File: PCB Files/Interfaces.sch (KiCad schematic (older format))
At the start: 22 parts

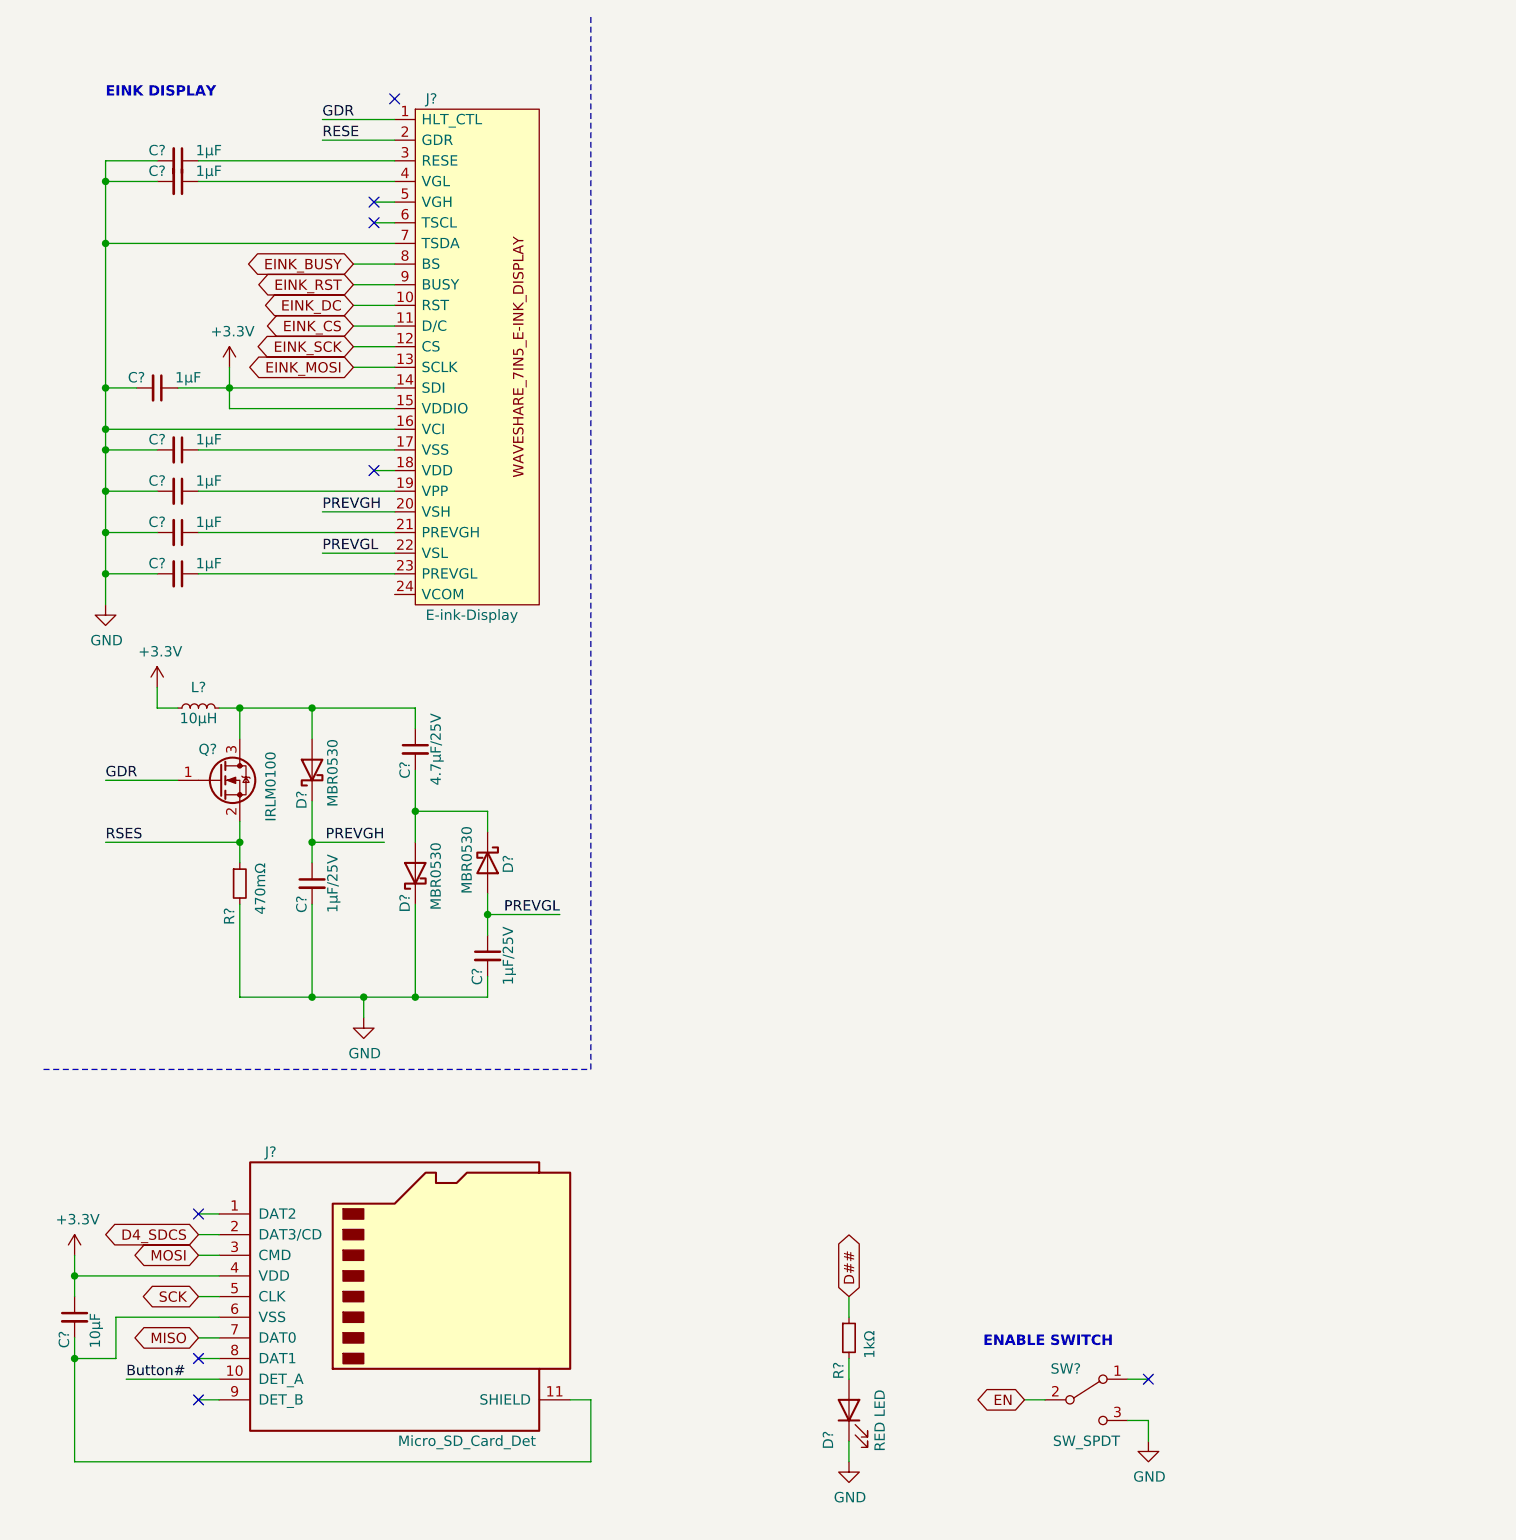
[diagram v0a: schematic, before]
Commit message: Added buttons, aux power distribution and connections to PI Pico
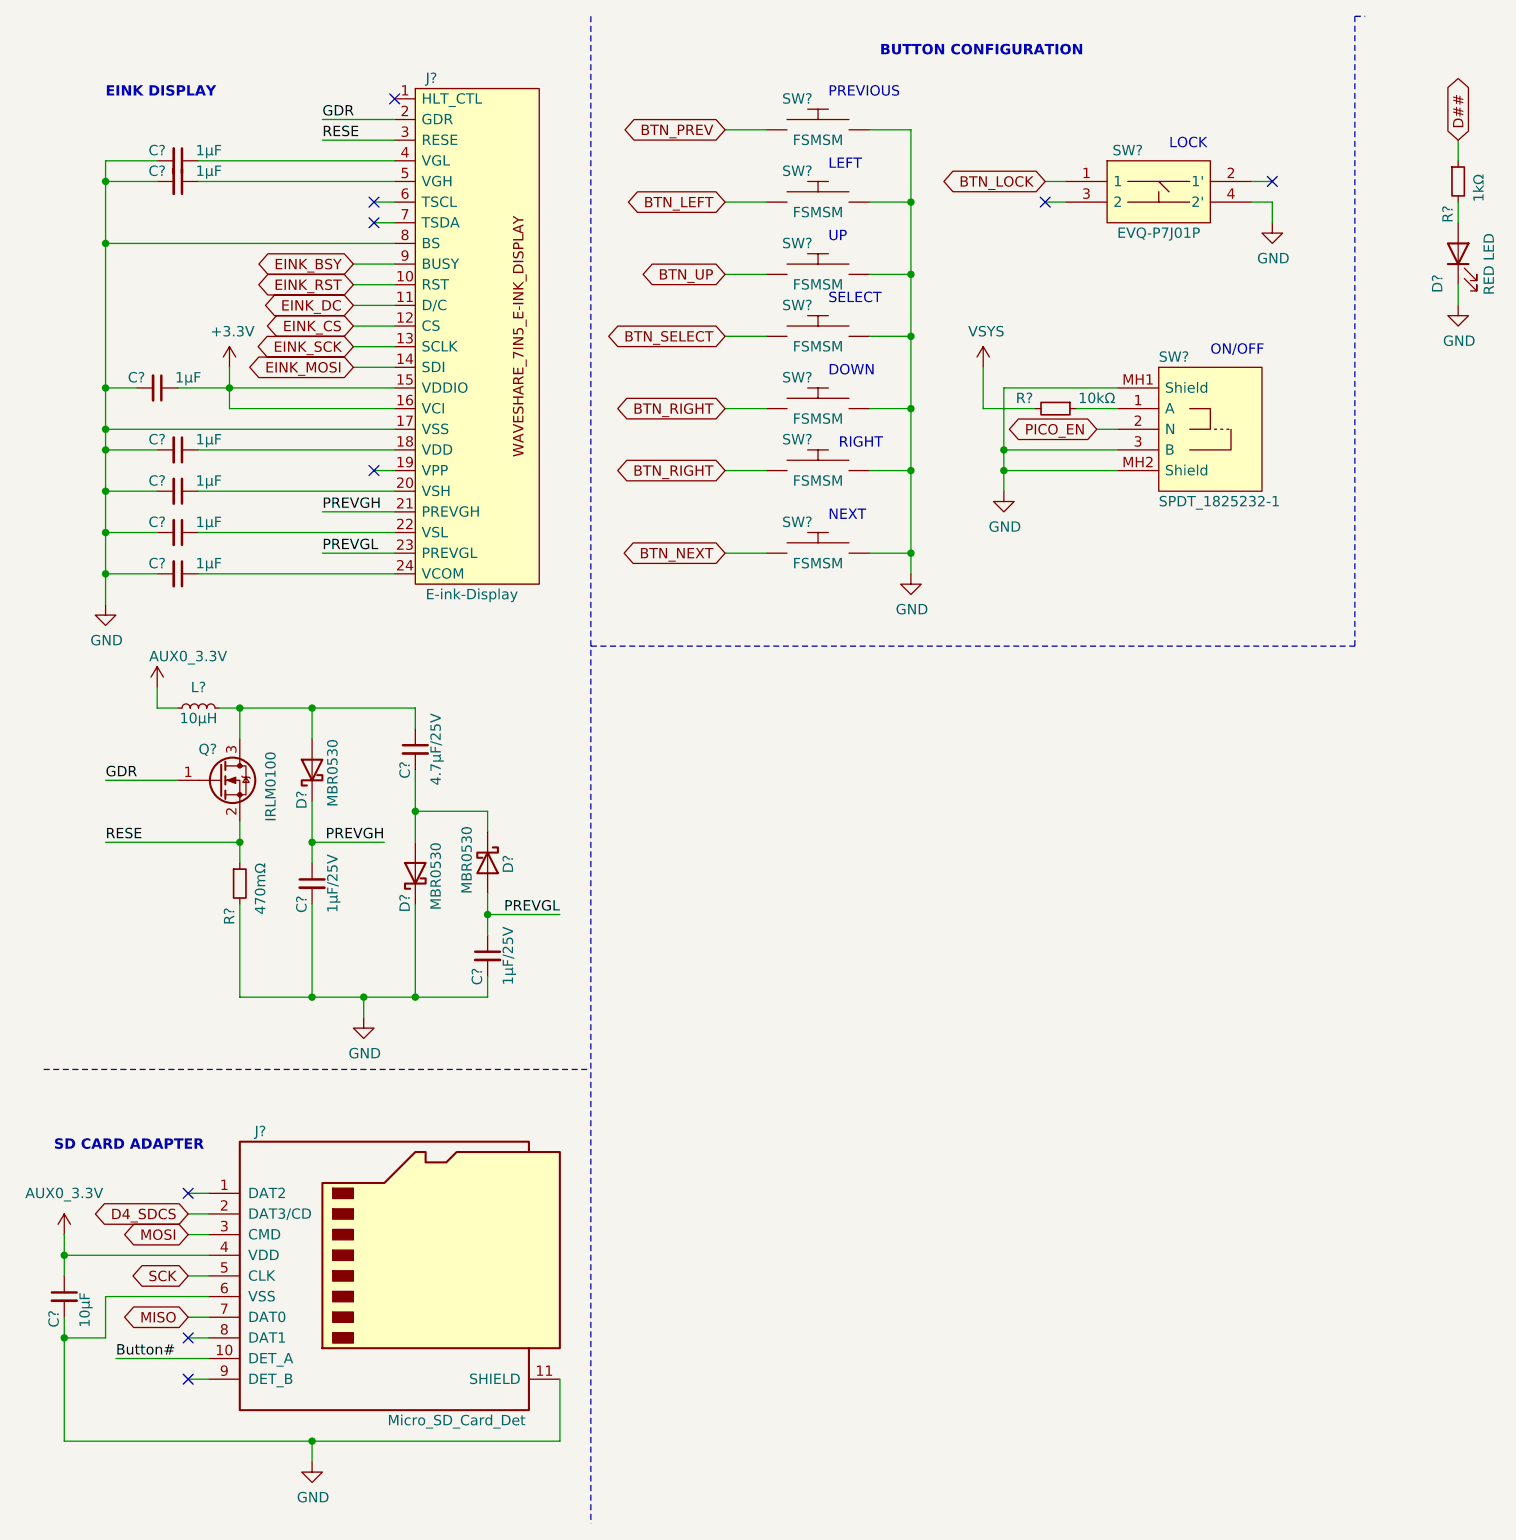
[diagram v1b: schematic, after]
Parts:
- removed SW?: SW_SPDT, symbol Switch:SW_SPDT
- added R?: 10kΩ, symbol Device:R_Small
- added SW? (x7): FSMSM, FSMSM, symbol E-ink-Pico:FSMSM
- added SW?: EVQ-P7J01P, EVQP7J01P, symbol E-ink-Pico:EVQ-P7J01P
- added SW?: SPDT_1825232-1, 18252321, symbol E-ink-Pico:SPDT_1825232-1
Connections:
- net EINK_BUSY is gone; now on net GND: J?.8 (BS)
- net RSES is gone; now on net RESE: Q?.2 (S), R?.1
- net +3V3: now also J?.16 (VCI); no longer C?.1, J?.14 (SDI), J?.4 (VDD), L?.1
- net EINK_CS: now also J?.12 (CS); no longer J?.11 (D/C)
- net EINK_DC: now also J?.11 (D/C); no longer J?.10 (RST)
- net EINK_MOSI: now also J?.14 (SDI); no longer J?.13 (SCLK)
- net EINK_RST: now also J?.10 (RST); no longer J?.9 (BUSY)
- net EINK_SCK: now also J?.13 (SCLK); no longer J?.12 (CS)
- net GDR: now also J?.2 (GDR); no longer J?.1 (HLT_CTL)
- net GND: now also C?.2, J?.11 (SHIELD), J?.17 (VSS), J?.6 (VSS), SW?.3 (B), SW?.4 (2'), SW?.MH1 (Shield), SW?.MH2 (Shield), SW?.~, SW?.~, SW?.~, SW?.~, SW?.~, SW?.~, SW?.~; no longer J?.16 (VCI), J?.7 (TSDA)
- net PREVGH: now also J?.21 (PREVGH); no longer J?.20 (VSH)
- net PREVGL: now also J?.23 (PREVGL); no longer J?.22 (VSL)
- net RESE: now also J?.3 (RESE); no longer J?.2 (GDR)
- net at C?.1: now also J?.4 (VGL); no longer J?.3 (RESE)
- net at C?.1: now also J?.5 (VGH); no longer J?.4 (VGL)
- net at C?.1: now also J?.18 (VDD); no longer J?.17 (VSS)
- net at C?.1: now also J?.20 (VSH); no longer J?.19 (VPP)
- net at C?.1: now also J?.22 (VSL); no longer J?.21 (PREVGH)
- net at C?.1: now also J?.24 (VCOM); no longer J?.23 (PREVGL)
- new net: R?.1, SW?.1 (A)
- new net BTN_LEFT: SW?.~
- new net BTN_LOCK: SW?.1
- new net BTN_NEXT: SW?.~
- new net BTN_PREV: SW?.~
- new net BTN_RIGHT: SW?.~, SW?.~
- new net BTN_SELECT: SW?.~
- new net BTN_UP: SW?.~
- new net EINK_BSY: J?.9 (BUSY)
- new net PICO_EN: SW?.2 (N)
- new net VCC: C?.1, J?.4 (VDD), L?.1, R?.2
- no-connect marks 8 -> 9
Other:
- note added: "BUTTON CONFIGURATION"
- note added: "DOWN"
- note added: "LEFT"
- note added: "LOCK"
- note added: "NEXT"
- note added: "ON/OFF"
- note added: "PREVIOUS"
- note added: "RIGHT"
- note added: "SD CARD ADAPTER"
- note added: "SELECT"
- note added: "UP"
- note removed: "ENABLE SWITCH"
- moved on the sheet: C?, D?, J?, R?
